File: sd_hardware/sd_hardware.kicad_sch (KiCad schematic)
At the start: 28 parts, among them IC1 BD9E201FP4-Z, J10 Conn_01x02_Socket, J11 RJ45, J2 RJ45, J3 Conn_01x02_Socket, J4 Conn_01x02_Socket, J5 Conn_01x02_Socket, J6 Conn_01x02_Socket, J7 Conn_01x02_Socket, J8 Conn_01x02_Socket, J9 Conn_01x02_Socket

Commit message: add sw
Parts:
- added SW2: SW_DIP_x03, symbol Switch:SW_DIP_x03
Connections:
- net GND: now also SW2.4, SW2.5, SW2.6
- net MCU_stm32_g431k8t6/ID_SW_BIT1: now also SW2.1
- net MCU_stm32_g431k8t6/ID_SW_BIT2: now also SW2.2
- net MCU_stm32_g431k8t6/ID_SW_BIT3: now also SW2.3
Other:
- sheet MCU_stm32_g431k8t6 ports: added none; removed ID_SW_BIT4
- moved on the sheet: C1, C2, J11, J2, PS1

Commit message: fix
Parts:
- added J11: XT60PW-M_1x02_Horizontal, Connector_AMASS:AMASS_XT60PW-M_1x02_P7.20mm_Horizontal, symbol y-robo:XT60PW-M_1x02_Horizontal
- added J12: Conn_01x02_Socket, Connector_JST:JST_XH_B2B-XH-AM_1x02_P2.50mm_Vertical, symbol Connector:Conn_01x02_Socket
- C10: renamed from C3; footprint (none) -> Capacitor_SMD:C_0603_1608Metric_Pad1.08x0.95mm_HandSolder
- C11: renamed from C4; footprint (none) -> Capacitor_SMD:C_0603_1608Metric_Pad1.08x0.95mm_HandSolder
- C12: renamed from C7; footprint (none) -> Capacitor_SMD:C_0603_1608Metric_Pad1.08x0.95mm_HandSolder
- C13: renamed from C8; footprint (none) -> Capacitor_SMD:C_0603_1608Metric_Pad1.08x0.95mm_HandSolder
- C14: renamed from C5; footprint (none) -> Capacitor_SMD:CP_Elec_10x12.6
- C7: renamed from C1; footprint (none) -> Capacitor_SMD:C_0603_1608Metric_Pad1.08x0.95mm_HandSolder
- C8: renamed from C2; footprint (none) -> Capacitor_SMD:C_0603_1608Metric_Pad1.08x0.95mm_HandSolder
- C9: renamed from C6; footprint (none) -> Capacitor_SMD:C_0603_1608Metric_Pad1.08x0.95mm_HandSolder
- D18: renamed from D1; footprint (none) -> LED_SMD:LED_0603_1608Metric_Pad1.05x0.95mm_HandSolder
- D19: footprint (none) -> LED_SMD:LED_0603_1608Metric_Pad1.05x0.95mm_HandSolder
- J1: renamed from J3; footprint (none) -> Connector_JST:JST_XH_B2B-XH-AM_1x02_P2.50mm_Vertical
- J10: renamed from J11; footprint (none) -> Connector_RJ:RJ45_Amphenol_54602-x08_Horizontal
- J2: renamed from J4; footprint (none) -> Connector_JST:JST_XH_B2B-XH-AM_1x02_P2.50mm_Vertical
- J3: renamed from J5; footprint (none) -> Connector_JST:JST_XH_B2B-XH-AM_1x02_P2.50mm_Vertical
- J4: renamed from J6; footprint (none) -> Connector_JST:JST_XH_B2B-XH-AM_1x02_P2.50mm_Vertical
- J5: renamed from J7; footprint (none) -> Connector_JST:JST_XH_B2B-XH-AM_1x02_P2.50mm_Vertical
- J6: renamed from J8; footprint (none) -> Connector_JST:JST_XH_B2B-XH-AM_1x02_P2.50mm_Vertical
- J7: renamed from J9; footprint (none) -> Connector_JST:JST_XH_B2B-XH-AM_1x02_P2.50mm_Vertical
- J8: renamed from J10; footprint (none) -> Connector_JST:JST_XH_B2B-XH-AM_1x02_P2.50mm_Vertical
- J9: renamed from J2; footprint (none) -> Connector_RJ:RJ45_Amphenol_54602-x08_Horizontal
- L1: footprint (none) -> Inductor_SMD:L_12x12mm_H4.5mm
- PS101: renamed from PS1; footprint SOT95P280X125-5N -> y-robo_footprint:SOT95P280X125-5N
- R10: renamed from R3; footprint (none) -> Resistor_SMD:R_0603_1608Metric_Pad0.98x0.95mm_HandSolder
- R11: renamed from R1; footprint (none) -> Resistor_SMD:R_0603_1608Metric_Pad0.98x0.95mm_HandSolder
- R12: footprint (none) -> Resistor_SMD:R_0603_1608Metric_Pad0.98x0.95mm_HandSolder
- R9: renamed from R2; footprint (none) -> Resistor_SMD:R_0603_1608Metric_Pad0.98x0.95mm_HandSolder
- SW1: renamed from SW2; footprint (none) -> y-robo_footprint:DS04-254-2-03BK-SMT
- renumbered D2 to D17, IC1 to IC101
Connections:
- net +24V: now also J11.1 (-)
- net CANH: now also J12.2 (Pin_2)
- net CANL: now also J12.1 (Pin_1)
- net GNDPWR: now also J11.2 (+)

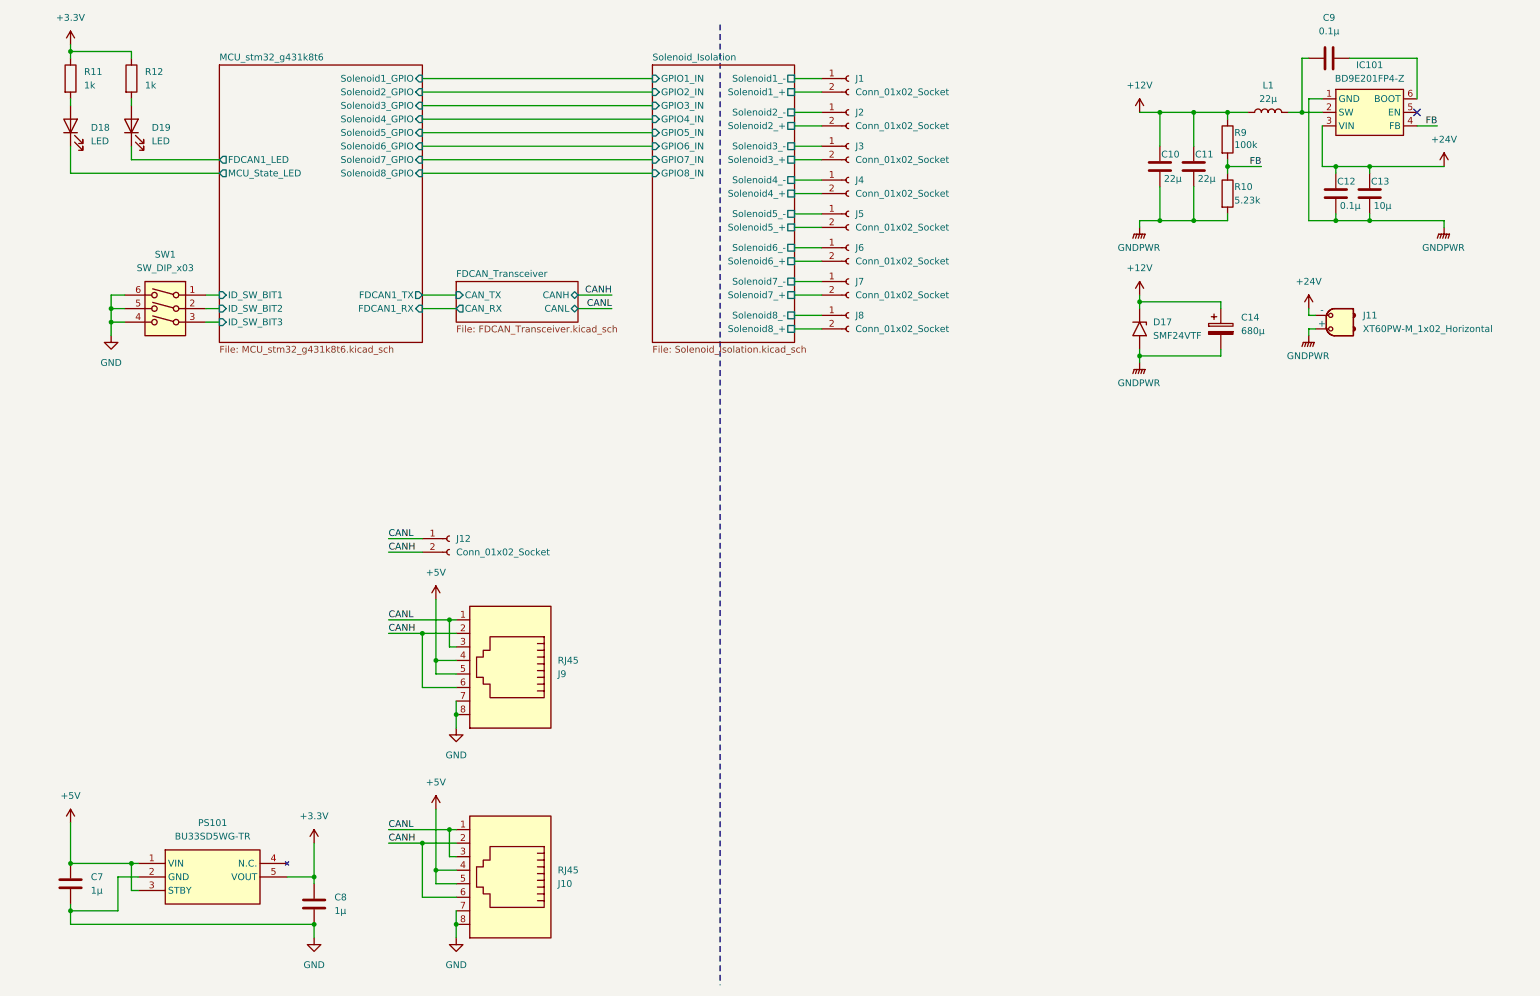
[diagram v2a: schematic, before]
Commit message: fix var3.0 sd_hardware
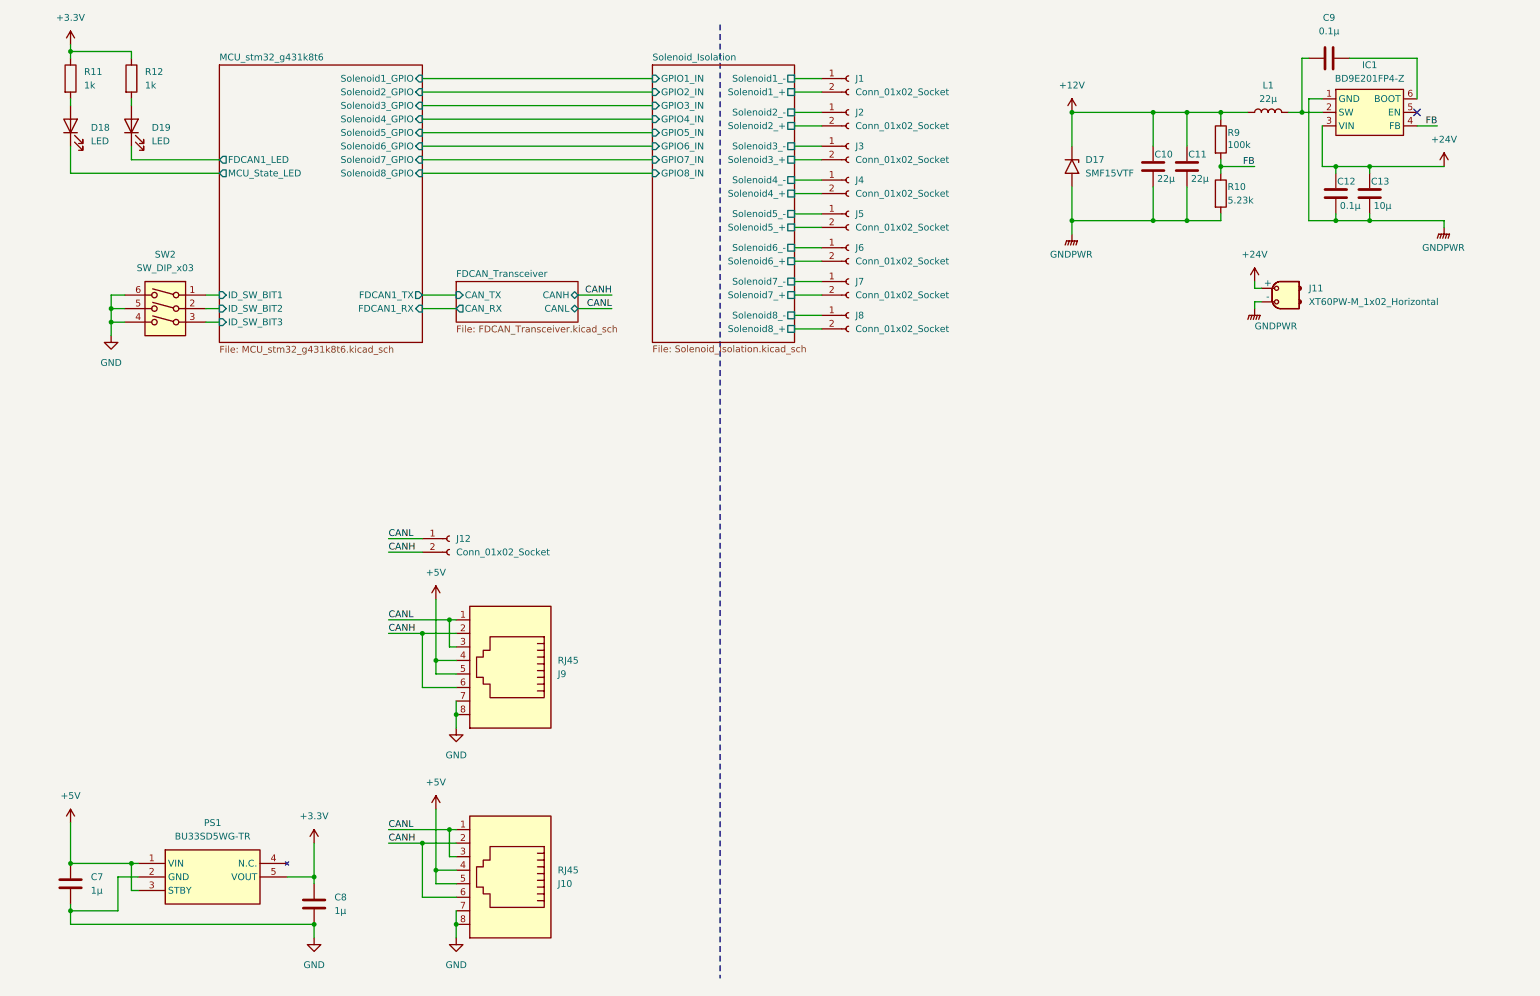
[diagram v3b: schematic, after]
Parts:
- removed C14: 680μ, Capacitor_SMD:CP_Elec_10x12.6, symbol Device:C_Polarized
- D17: value SMF24VTF -> SMF15VTF
- L1: footprint Inductor_SMD:L_12x12mm_H4.5mm -> y-robo_footprint:RP1315BNP-220M
- renumbered IC101 to IC1, PS101 to PS1, SW1 to SW2
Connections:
- net +24V: now also J11.2 (+); no longer J11.1 (-)
- net GNDPWR: now also J11.1 (-); no longer J11.2 (+)
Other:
- moved on the sheet: C10, C11, J11, R10, R9

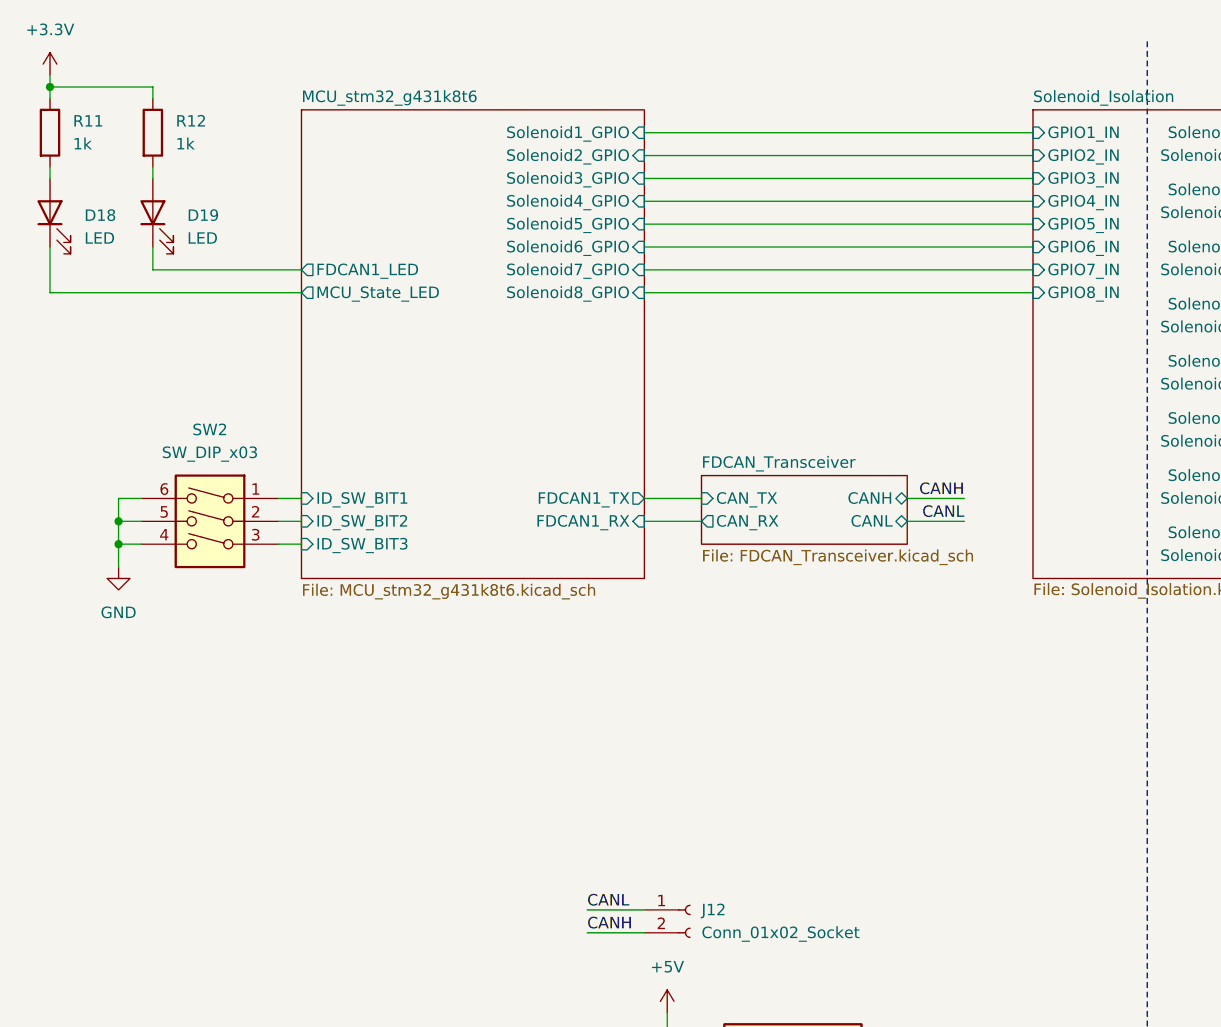
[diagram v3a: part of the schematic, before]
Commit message: Change to Photo Relay
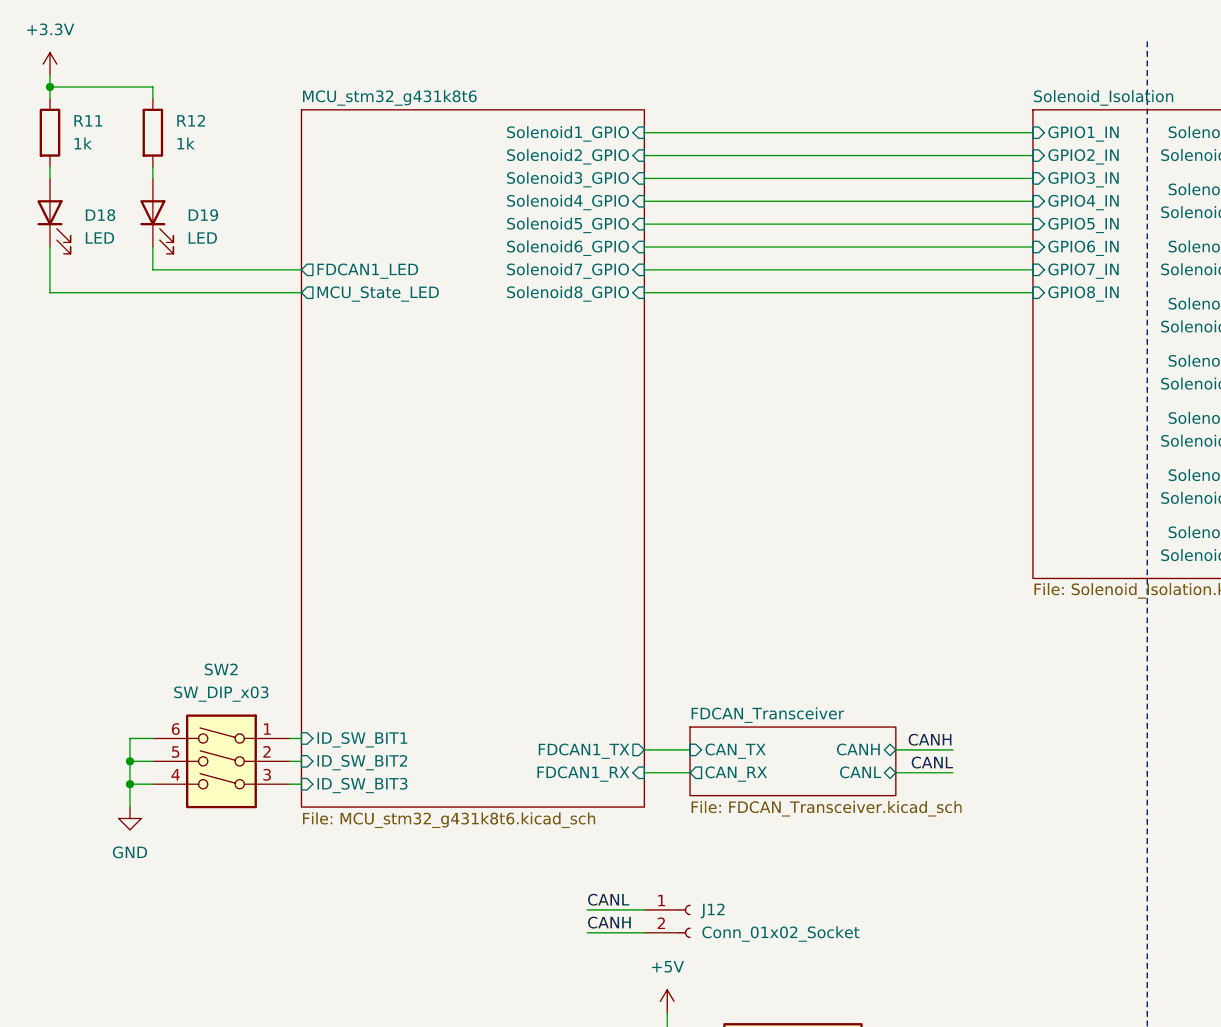
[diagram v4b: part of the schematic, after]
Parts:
- J1: footprint Connector_JST:JST_XH_B2B-XH-AM_1x02_P2.50mm_Vertical -> Connector_JST:JST_XH_B2B-XH-A_1x02_P2.50mm_Vertical
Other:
- moved on the sheet: SW2
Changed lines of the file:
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@@
 	)
 	(junction
-		(at 31.75 72.39)
+		(at 33.02 99.06)
 		(diameter 0)
 		(color 0 0 0 0)
@@
 	)
 	(junction
-		(at 31.75 69.85)
+		(at 33.02 96.52)
 		(diameter 0)
 		(color 0 0 0 0)
@@
 	(wire
 		(pts
-			(xy 31.75 72.39) (xy 34.29 72.39)
+			(xy 33.02 99.06) (xy 35.56 99.06)
 		)
 		(stroke
@@
 	(wire
 		(pts
-			(xy 119.38 67.31) (xy 125.73 67.31)
+			(xy 118.11 95.25) (xy 124.46 95.25)
 		)
 		(stroke
@@
 	(wire
 		(pts
-			(xy 31.75 74.93) (xy 31.75 72.39)
+			(xy 33.02 101.6) (xy 33.02 99.06)
 		)
 		(stroke
@@
 	(wire
 		(pts
-			(xy 31.75 67.31) (xy 34.29 67.31)
+			(xy 33.02 93.98) (xy 35.56 93.98)
 		)
 		(stroke
@@
 	(wire
 		(pts
-			(xy 31.75 69.85) (xy 31.75 72.39)
+			(xy 33.02 96.52) (xy 33.02 99.06)
 		)
 		(stroke
@@
 	(wire
 		(pts
-			(xy 31.75 67.31) (xy 31.75 69.85)
+			(xy 33.02 93.98) (xy 33.02 96.52)
 		)
 		(stroke
@@
 	(wire
 		(pts
-			(xy 49.53 69.85) (xy 52.07 69.85)
+			(xy 50.8 96.52) (xy 52.07 96.52)
 		)
 		(stroke
@@
 	(wire
 		(pts
-			(xy 119.38 69.85) (xy 125.73 69.85)
+			(xy 118.11 97.79) (xy 124.46 97.79)
 		)
 		(stroke
@@
 	(wire
 		(pts
-			(xy 49.53 72.39) (xy 52.07 72.39)
+			(xy 50.8 99.06) (xy 52.07 99.06)
 		)
 		(stroke
@@
 	(wire
 		(pts
-			(xy 49.53 67.31) (xy 52.07 67.31)
+			(xy 50.8 93.98) (xy 52.07 93.98)
 		)
 		(stroke
@@
 	(wire
 		(pts
-			(xy 90.17 69.85) (xy 96.52 69.85)
+			(xy 90.17 97.79) (xy 95.25 97.79)
 		)
 		(stroke
@@
 	(wire
 		(pts
-			(xy 31.75 69.85) (xy 34.29 69.85)
+			(xy 33.02 96.52) (xy 35.56 96.52)
 		)
 		(stroke
@@
 	(wire
 		(pts
-			(xy 90.17 67.31) (xy 96.52 67.31)
+			(xy 90.17 95.25) (xy 95.25 95.25)
 		)
 		(stroke
@@
 	)
 	(label "CANH"
-		(at 125.73 67.31 180)
+		(at 124.46 95.25 180)
 		(effects
 			(font
@@
 	)
 	(label "CANL"
-		(at 125.73 69.85 180)
+		(at 124.46 97.79 180)
 		(effects
 			(font
@@
 	(symbol
 		(lib_id "Switch:SW_DIP_x03")
-		(at 41.91 69.85 0)
+		(at 43.18 96.52 0)
 		(mirror y)
 		(unit 1)
@@
 		(dnp no)
 		(property "Reference" "SW2"
-			(at 41.91 59.69 0)
+			(at 43.18 86.36 0)
 			(show_name no)
 			(do_not_autoplace no)
@@
 		)
 		(property "Value" "SW_DIP_x03"
-			(at 41.91 62.23 0)
+			(at 43.18 88.9 0)
 			(show_name no)
 			(do_not_autoplace no)
@@
 		)
 		(property "Footprint" "y-robo_footprint:DS04-254-2-03BK-SMT"
-			(at 41.91 72.39 0)
+			(at 43.18 99.06 0)
 			(hide yes)
 			(show_name no)
@@
 		)
 		(property "Datasheet" ""
-			(at 41.91 72.39 0)
+			(at 43.18 99.06 0)
 			(hide yes)
 			(show_name no)
@@
 		)
 		(property "Description" "3x DIP Switch, Single Pole Single Throw (SPST) switch, small symbol"
-			(at 41.91 69.85 0)
+			(at 43.18 96.52 0)
 			(hide yes)
 			(show_name no)
@@
 	(symbol
 		(lib_id "power:GND")
-		(at 31.75 74.93 0)
+		(at 33.02 101.6 0)
 		(unit 1)
 		(body_style 1)
@@
 		(fields_autoplaced yes)
 		(property "Reference" "#PWR0107"
-			(at 31.75 81.28 0)
+			(at 33.02 107.95 0)
 			(hide yes)
 			(show_name no)
@@
 		)
 		(property "Value" "GND"
-			(at 31.75 80.01 0)
+			(at 33.02 106.68 0)
 			(show_name no)
 			(do_not_autoplace no)
@@
 		)
 		(property "Footprint" ""
-			(at 31.75 74.93 0)
+			(at 33.02 101.6 0)
 			(hide yes)
 			(show_name no)
@@
 		)
 		(property "Datasheet" ""
-			(at 31.75 74.93 0)
+			(at 33.02 101.6 0)
 			(hide yes)
 			(show_name no)
@@
 		)
 		(property "Description" "Power symbol creates a global label with name \"GND\" , ground"
-			(at 31.75 74.93 0)
+			(at 33.02 101.6 0)
 			(hide yes)
 			(show_name no)
@@
 			)
 		)
-		(property "Footprint" "Connector_JST:JST_XH_B2B-XH-AM_1x02_P2.50mm_Vertical"
+		(property "Footprint" "Connector_JST:JST_XH_B2B-XH-A_1x02_P2.50mm_Vertical"
 			(at 170.18 26.67 0)
 			(hide yes)
@@
 	(sheet
 		(at 52.07 24.13)
-		(size 38.1 52.07)
+		(size 38.1 77.47)
 		(exclude_from_sim no)
 		(in_bom yes)
@@
 		)
 		(property "Sheetfile" "MCU_stm32_g431k8t6.kicad_sch"
-			(at 52.07 76.7846 0)
+			(at 52.07 102.1846 0)
 			(show_name no)
 			(do_not_autoplace no)
@@
 		)
 		(pin "FDCAN1_RX" input
-			(at 90.17 69.85 0)
+			(at 90.17 97.79 0)
 			(effects
 				(font
@@
 		)
 		(pin "FDCAN1_TX" output
-			(at 90.17 67.31 0)
+			(at 90.17 95.25 0)
 			(effects
 				(font
@@
 		)
 		(pin "ID_SW_BIT1" input
-			(at 52.07 67.31 180)
+			(at 52.07 93.98 180)
 			(effects
 				(font
@@
 		)
 		(pin "ID_SW_BIT2" input
-			(at 52.07 69.85 180)
+			(at 52.07 96.52 180)
 			(effects
 				(font
@@
 		)
 		(pin "ID_SW_BIT3" input
-			(at 52.07 72.39 180)
+			(at 52.07 99.06 180)
 			(effects
 				(font
@@
 	)
 	(sheet
-		(at 96.52 64.77)
+		(at 95.25 92.71)
 		(size 22.86 7.62)
 		(exclude_from_sim no)
@@
 		)
 		(property "Sheetname" "FDCAN_Transceiver"
-			(at 96.52 64.0584 0)
+			(at 95.25 91.9984 0)
 			(show_name no)
 			(do_not_autoplace no)
@@
 		)
 		(property "Sheetfile" "FDCAN_Transceiver.kicad_sch"
-			(at 96.52 72.9746 0)
+			(at 95.25 100.9146 0)
 			(show_name no)
 			(do_not_autoplace no)
@@
 		)
 		(pin "CANH" bidirectional
-			(at 119.38 67.31 0)
+			(at 118.11 95.25 0)
 			(effects
 				(font
@@
 		)
 		(pin "CANL" bidirectional
-			(at 119.38 69.85 0)
+			(at 118.11 97.79 0)
 			(effects
 				(font
@@
 		)
 		(pin "CAN_RX" output
-			(at 96.52 69.85 180)
+			(at 95.25 97.79 180)
 			(effects
 				(font
@@
 		)
 		(pin "CAN_TX" input
-			(at 96.52 67.31 180)
+			(at 95.25 95.25 180)
 			(effects
 				(font

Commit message: work
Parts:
- added J15: Conn_01x06_Socket, symbol Connector:Conn_01x06_Socket
- added R6, R7: 0, symbol Device:R
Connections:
- net +12V: now also J15.1 (Pin_1)
- net GNDPWR: now also J15.2 (Pin_2)
- net MCU_stm32_g431k8t6/ID_SW_BIT3: no longer SW2.3
- new net MCU_stm32_g431k8t6/SPI1_MOSI: R7.1
- new net MCU_stm32_g431k8t6/SPI1_SCK: R6.1
- new net SPI_DAC/+VSENSE: J15.5 (Pin_5)
- new net SPI_DAC/-VSENSE: J15.3 (Pin_3)
- new net SPI_DAC/VOUT: J15.4 (Pin_4)
- new net SPI_Iso/CLK_IN: R6.2
- new net SPI_Iso/MOSI_IN: R7.2
- no-connect marks 1 -> 3
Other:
- sheet Solenoid_Isolation renamed Solenoid_Iso
- added sheet SPI_ADC (SPI_ADC.kicad_sch)
- added sheet SPI_DAC (SPI_DAC.kicad_sch)
- added sheet SPI_Iso (SPI_Iso.kicad_sch)
- sheet MCU_stm32_g431k8t6 ports: added EP_Regu_LATCH, SPI1_MISO, SPI1_MOSI, SPI1_SCK; removed none
- sheet Solenoid_Iso: file Solenoid_Isolation.kicad_sch -> Solenoid_Iso.kicad_sch
- note added: "1. Brown Vs(+12V) 2. Blue GND 3. -VSENSE 4. White Vin(DAC OUT) 5. +VSENSE 6. Black Monitor"
- moved on the sheet: J10, J12, J9, SW2
